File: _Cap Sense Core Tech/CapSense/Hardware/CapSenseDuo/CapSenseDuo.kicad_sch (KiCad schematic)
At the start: 39 parts, among them IC1 FDC2214-rescue_FDC2214QRGHRQ1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, IC2 FDC2214QRGHRQ1, J1 Conn_01x08, J2 Conn_01x08, Y1 ECS-2033-400-BN

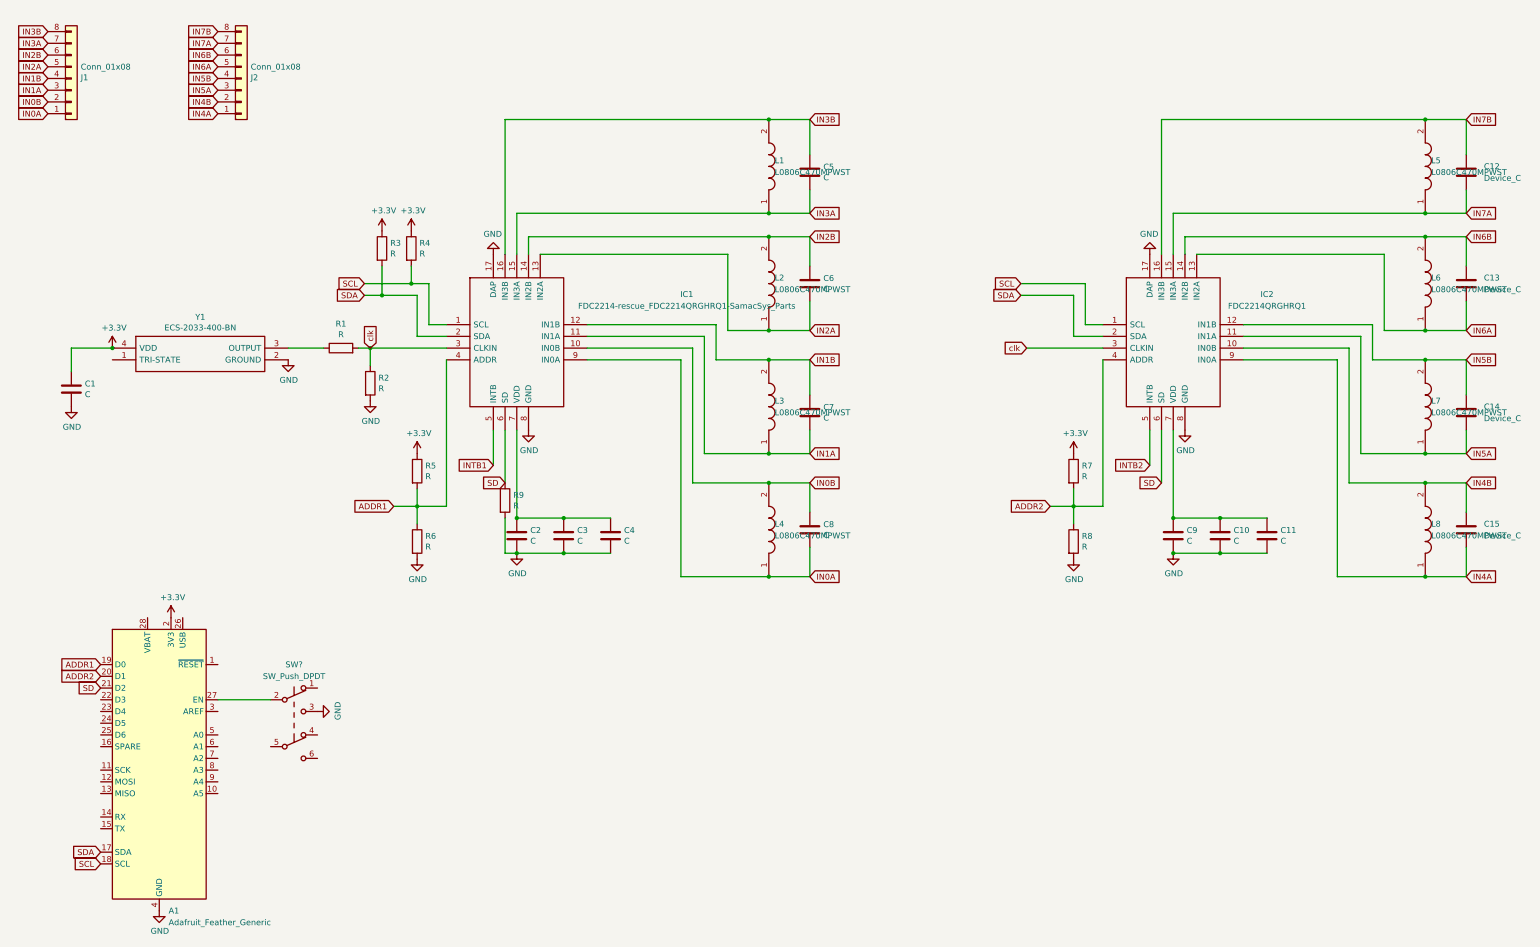
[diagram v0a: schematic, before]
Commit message: place and route finished for CapDuo
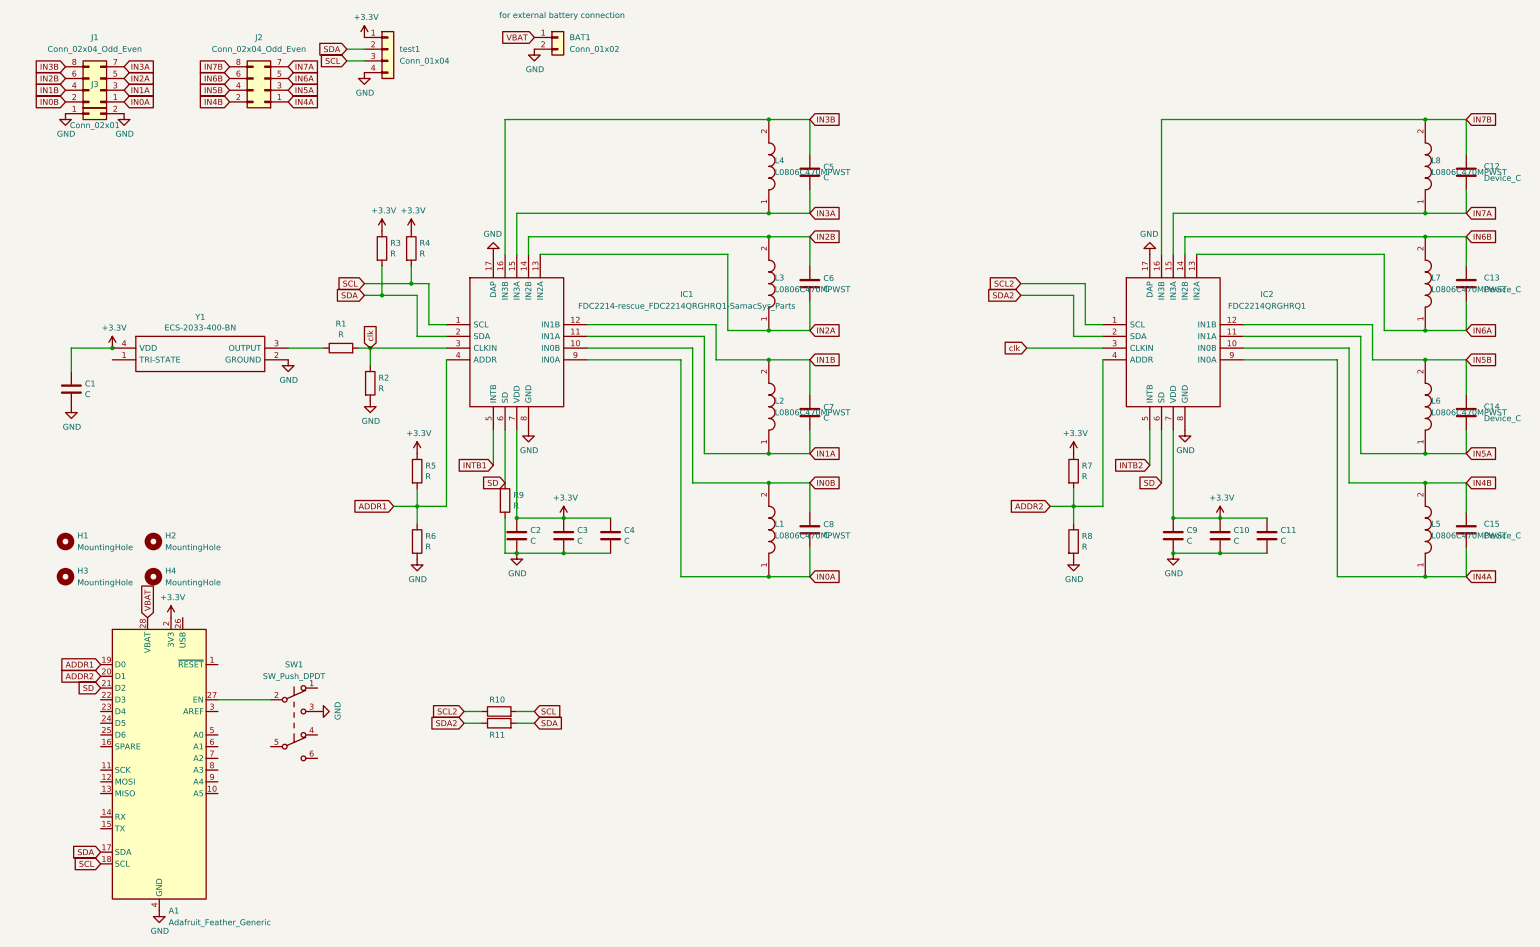
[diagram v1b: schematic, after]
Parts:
- removed J1, J2: Conn_01x08, Connector_PinHeader_2.54mm:PinHeader_1x08_P2.54mm_Vertical, symbol Connector_Generic:Conn_01x08
- added BAT1: Conn_01x02, Connector_PinHeader_2.54mm:PinHeader_1x02_P2.54mm_Vertical, symbol Connector_Generic:Conn_01x02
- added H1, H2, H3, H4: MountingHole, MountingHole:MountingHole_2.7mm_M2.5, symbol Mechanical:MountingHole
- added J1, J2: Conn_02x04_Odd_Even, Connector_PinHeader_2.54mm:PinHeader_2x04_P2.54mm_Horizontal, symbol Connector_Generic:Conn_02x04_Odd_Even
- added J3: Conn_02x01, Connector_PinHeader_2.54mm:PinHeader_2x01_P2.54mm_Horizontal, symbol Connector_Generic:Conn_02x01
- added R10, R11: R, Resistor_SMD:R_0603_1608Metric_Pad0.98x0.95mm_HandSolder, symbol Device:R
- added test1: Conn_01x04, Connector_PinHeader_2.00mm:PinHeader_1x04_P2.00mm_Vertical, symbol Connector_Generic:Conn_01x04
- gave numbers to parts that had none: 1
- renumbered L4 to L1, L3 to L2, L2 to L3, L1 to L4, L8 to L5, L7 to L6, L6 to L7, L5 to L8
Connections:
- net +3V3: now also C10.1, C11.1, C2.1, C3.1, C4.1, C9.1, IC1.7 (VDD), IC2.7 (VDD), test1.1 (Pin_1)
- net GND: now also BAT1.2 (Pin_2), J3.1 (Pin_1), J3.2 (Pin_2), test1.4 (Pin_4)
- net IN0A: now also J1.1 (Pin_1)
- net IN0B: now also J1.2 (Pin_2)
- net IN1A: now also J1.3 (Pin_3)
- net IN1B: now also J1.4 (Pin_4)
- net IN2A: now also J1.5 (Pin_5)
- net IN2B: now also J1.6 (Pin_6)
- net IN3A: now also J1.7 (Pin_7)
- net IN3B: now also J1.8 (Pin_8)
- net IN4A: now also J2.1 (Pin_1)
- net IN4B: now also J2.2 (Pin_2)
- net IN5A: now also J2.3 (Pin_3)
- net IN5B: now also J2.4 (Pin_4)
- net IN6A: now also J2.5 (Pin_5)
- net IN6B: now also J2.6 (Pin_6)
- net IN7A: now also J2.7 (Pin_7)
- net IN7B: now also J2.8 (Pin_8)
- net SCL: now also R10.2, test1.3 (Pin_3); no longer IC2.1 (SCL)
- net SDA: now also R11.2, test1.2 (Pin_2); no longer IC2.2 (SDA)
- net VBAT: now reaches A1.28 (VBAT)
- net VBAT: now also BAT1.1 (Pin_1)
- new net SCL2: IC2.1 (SCL), R10.1
- new net SDA2: IC2.2 (SDA), R11.1
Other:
- note added: "for external battery connection"
